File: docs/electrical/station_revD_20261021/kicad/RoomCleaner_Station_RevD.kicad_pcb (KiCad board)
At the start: 2 copper layers, 70 x 50 mm, 14 parts, among them J1 12V_IN, J2 MOTOR_NEMA17, J3 SWITCH_KW12-3, J5 ENCODER_AS5600, U1 DROK_buck_5.00V, U2 XIAO_ESP32C3, U3 A4988_carrier

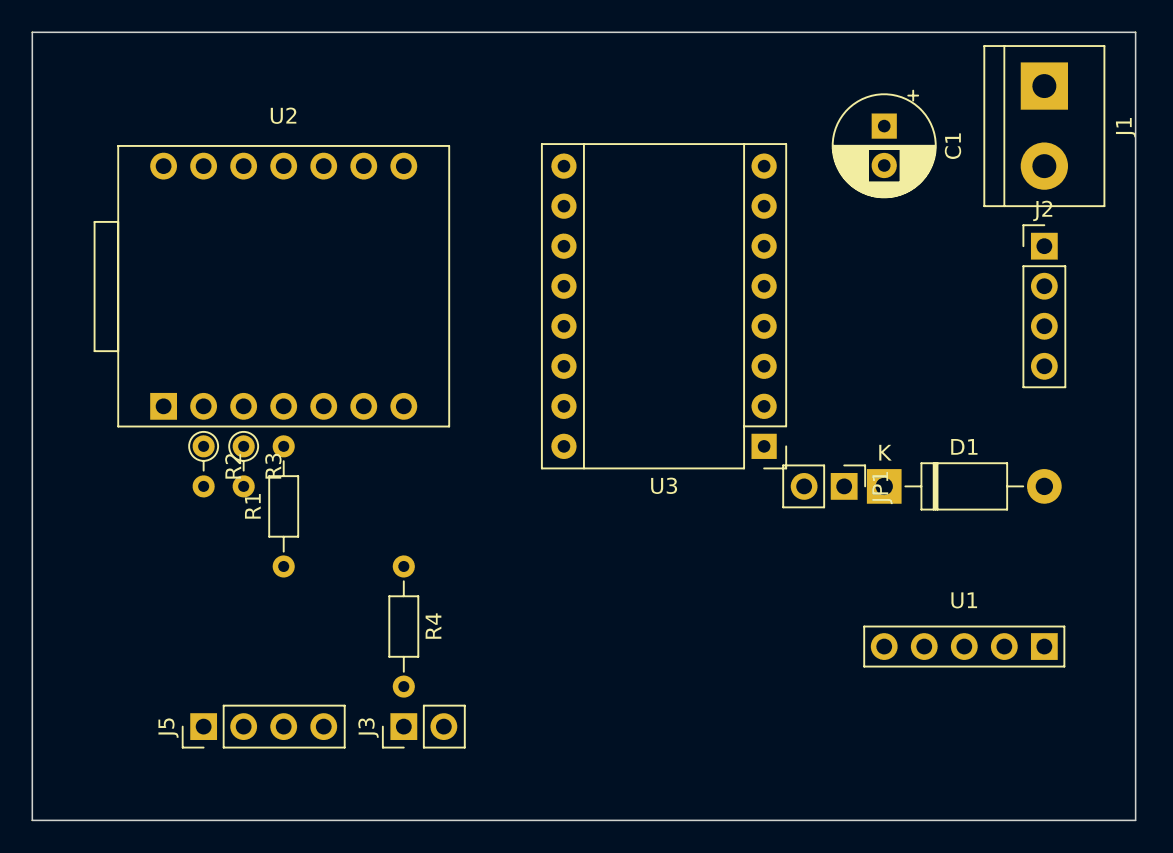
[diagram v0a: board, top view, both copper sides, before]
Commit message: Station Rev D KiCad project: schematic (ERC 0/0), netlist matches perfboard (16 nets, PASS), placed 70x50 mm PCB (DRC: unrouted only), generator and checks
Co-Authored-By: Claude Opus 5.5 <noreply@anthropic.com>
Claude-Session: https://claude.ai/code/session_012vxDhJBdXDDzxaEvKJXH5D
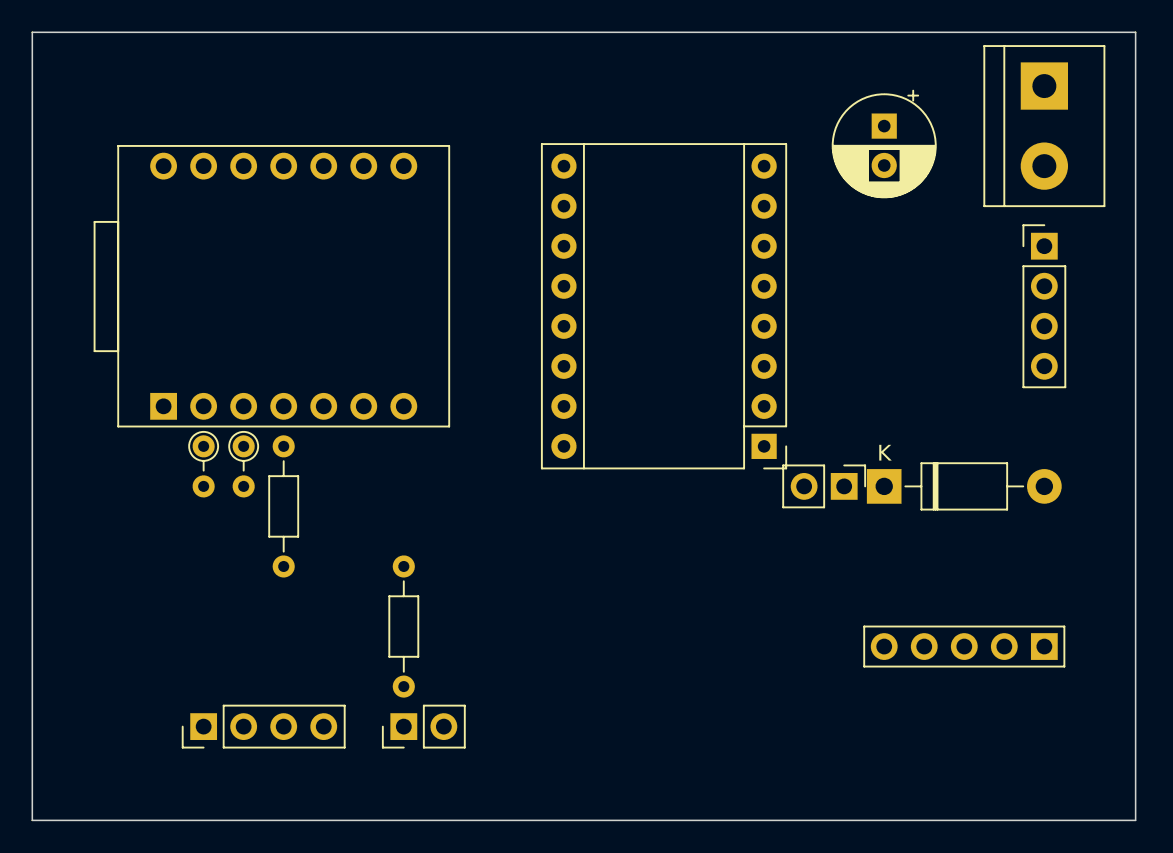
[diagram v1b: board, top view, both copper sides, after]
